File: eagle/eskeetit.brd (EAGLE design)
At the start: 47 x 28 mm, 46 parts, among them M1 WIRELESS-NRF24L01, U1 GY-521MPU6050, U2 TPS63000DRCR, Y1 20MHz

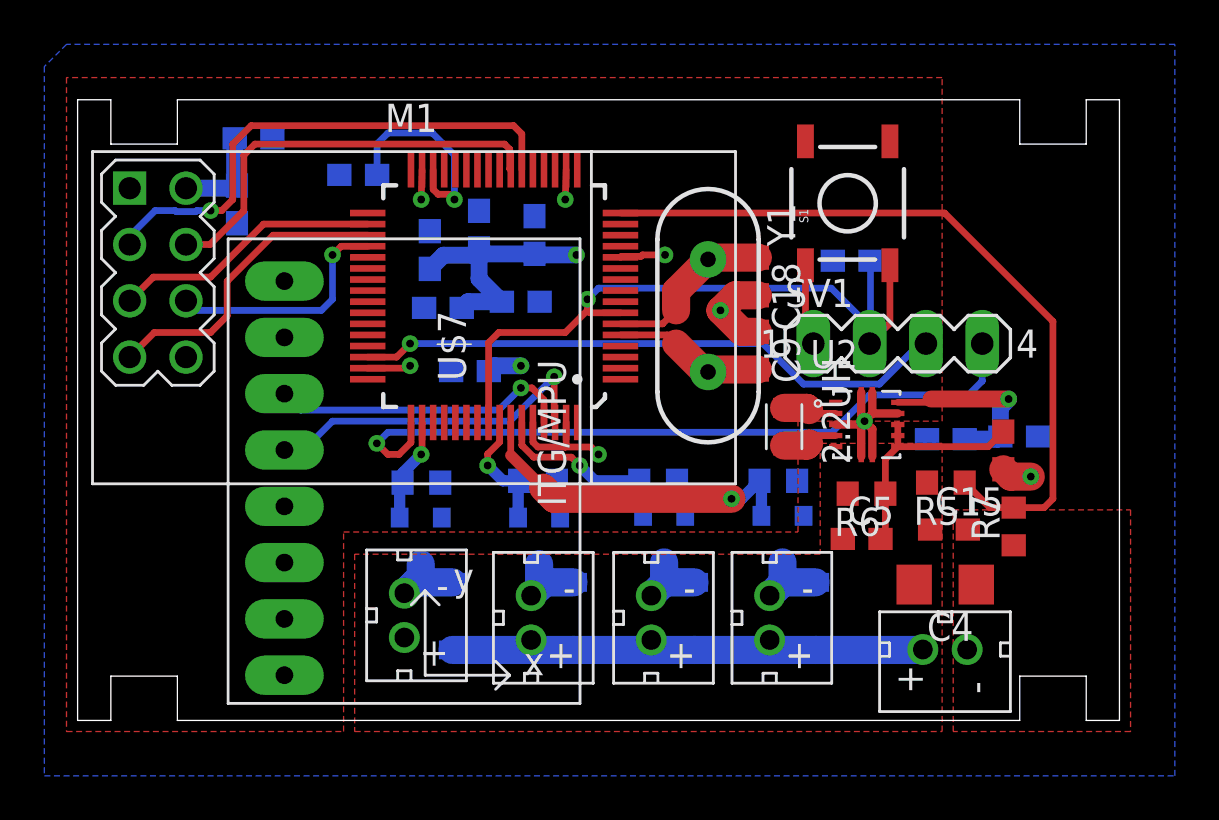
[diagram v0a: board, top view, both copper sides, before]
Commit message: changed PA5 to 20 mils, fixed some bottlenecks
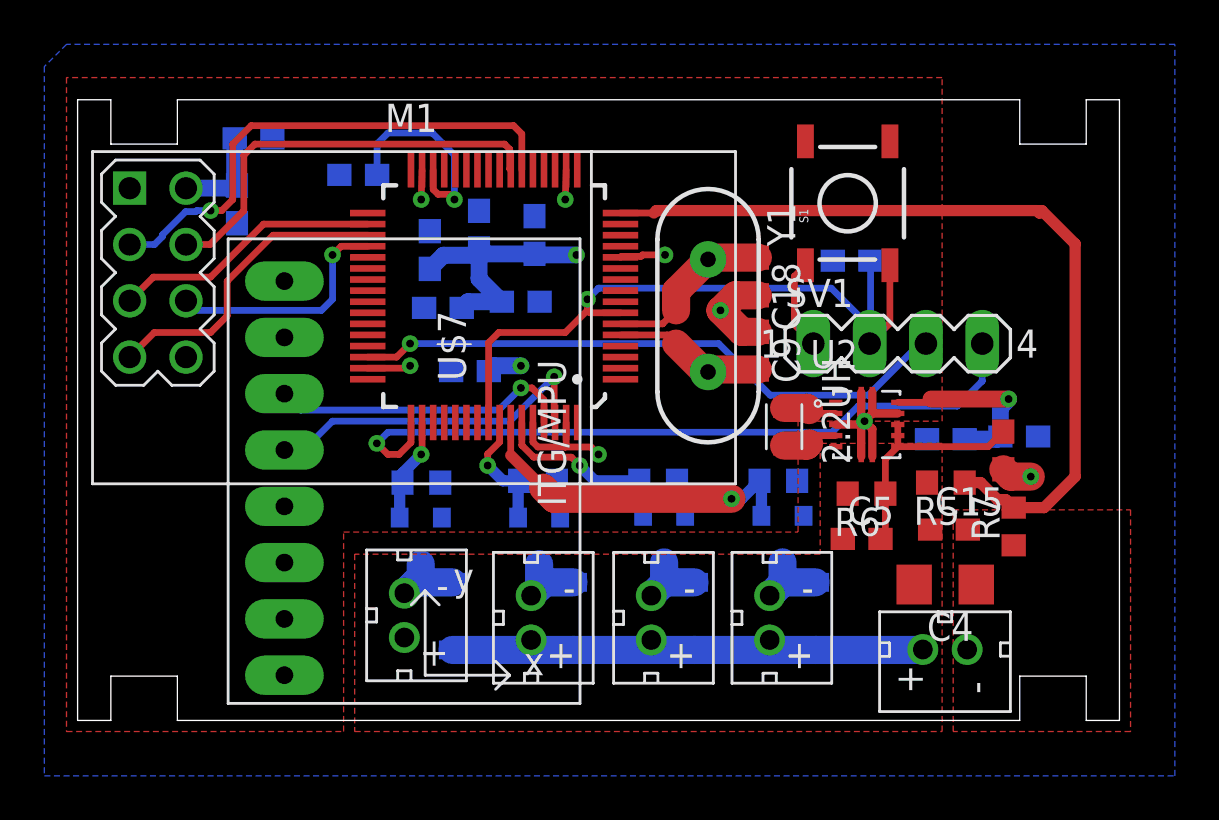
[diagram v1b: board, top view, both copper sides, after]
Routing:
- net PA5: track 34.1 -> 37.8 mm
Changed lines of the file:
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@@
 </polygon>
 <contactref element="SV1" pad="1"/>
-<wire x1="32.835" y1="20.536" x2="32.835" y2="17.355" width="0.3048" layer="1"/>
-<wire x1="32.835" y1="17.355" x2="33.19" y2="17" width="0.3048" layer="1"/>
+<wire x1="32.835" y1="20.536" x2="32.335" y2="20.036" width="0.3048" layer="1"/>
+<wire x1="32.335" y1="20.036" x2="32.335" y2="17.855" width="0.3048" layer="1"/>
+<wire x1="32.335" y1="17.855" x2="33.19" y2="17" width="0.3048" layer="1"/>
 <wire x1="13.09" y1="15.89" x2="14.89" y2="15.89" width="0.3048" layer="1"/>
 <wire x1="14.89" y1="15.89" x2="15" y2="16" width="0.3048" layer="1"/>
@@
 <contactref element="SV1" pad="3"/>
 <wire x1="38.27" y1="17" x2="38.0006875" y2="17" width="0.3048" layer="16"/>
-<wire x1="30.9193125" y1="17" x2="15" y2="17" width="0.3048" layer="16"/>
-<wire x1="38.0006875" y1="17" x2="36.1718875" y2="15.1712" width="0.3048" layer="16"/>
-<wire x1="32.7481125" y1="15.1712" x2="30.9193125" y2="17" width="0.3048" layer="16"/>
-<wire x1="36.1718875" y1="15.1712" x2="32.7481125" y2="15.1712" width="0.3048" layer="16"/>
+<wire x1="28.9193125" y1="17" x2="15" y2="17" width="0.3048" layer="16"/>
+<wire x1="38.0006875" y1="17" x2="35.6718875" y2="14.6712" width="0.3048" layer="16"/>
+<wire x1="31.2481125" y1="14.6712" x2="28.9193125" y2="17" width="0.3048" layer="16"/>
+<wire x1="35.6718875" y1="14.6712" x2="31.2481125" y2="14.6712" width="0.3048" layer="16"/>
 <via x="15" y="17" extent="1-16" drill="0.35"/>
 <wire x1="15" y1="17" x2="14.39" y2="16.39" width="0.3048" layer="1"/>
@@
 <contactref element="U$7" pad="49"/>
 <contactref element="SV1" pad="4"/>
-<wire x1="34.0340875" y1="13" x2="35.7170875" y2="14.683" width="0.3048" layer="16"/>
+<wire x1="34.0340875" y1="13" x2="35.2170875" y2="14.183" width="0.3048" layer="16"/>
 <wire x1="34.0340875" y1="13" x2="14" y2="13" width="0.3048" layer="16"/>
 <wire x1="14" y1="13" x2="13.5" y2="12.5" width="0.3048" layer="16"/>
@@
 <wire x1="15.04" y1="12.54" x2="15.04" y2="13.44" width="0.3048" layer="1"/>
 <wire x1="14.5" y1="12" x2="15.04" y2="12.54" width="0.3048" layer="1"/>
-<wire x1="35.7170875" y1="14.683" x2="40.183" y2="14.683" width="0.3048" layer="16"/>
+<wire x1="35.2170875" y1="14.183" x2="39.683" y2="14.183" width="0.3048" layer="16"/>
 <wire x1="40.81" y1="15.31" x2="40.81" y2="17" width="0.3048" layer="16"/>
-<wire x1="40.183" y1="14.683" x2="40.81" y2="15.31" width="0.3048" layer="16"/>
+<wire x1="39.683" y1="14.183" x2="40.81" y2="15.31" width="0.3048" layer="16"/>
 </signal>
 <signal name="SWDRST">
@@
 <wire x1="6.5" y1="23" x2="6" y2="23" width="0.3048" layer="1"/>
 <via x="6" y="23" extent="1-16" drill="0.35"/>
-<wire x1="6" y1="23" x2="5.377375" y2="23" width="0.3048" layer="16"/>
-<wire x1="5.377375" y1="23" x2="5.328575" y2="22.9512" width="0.3048" layer="16"/>
-<wire x1="5.328575" y1="22.9512" x2="4.451425" y2="22.9512" width="0.3048" layer="16"/>
-<wire x1="4.451425" y1="22.9512" x2="4.402625" y2="23" width="0.3048" layer="16"/>
-<wire x1="4.402625" y1="23" x2="3.5" y2="23" width="0.3048" layer="16"/>
-<wire x1="3.5" y1="23" x2="2.35" y2="21.85" width="0.3048" layer="16"/>
-<wire x1="2.35" y1="21.85" x2="2.35" y2="21.47" width="0.3048" layer="16"/>
+<wire x1="2.35" y1="21.47" x2="3.47" y2="21.47" width="0.3048" layer="16"/>
+<wire x1="3.47" y1="21.47" x2="3.8312" y2="21.8312" width="0.3048" layer="16"/>
+<wire x1="3.8312" y1="21.8312" x2="3.8312" y2="21.908575" width="0.3048" layer="16"/>
+<wire x1="3.8312" y1="21.908575" x2="4.873825" y2="22.9512" width="0.3048" layer="16"/>
+<wire x1="5.328575" y1="22.9512" x2="5.377375" y2="23" width="0.3048" layer="16"/>
+<wire x1="5.377375" y1="23" x2="6" y2="23" width="0.3048" layer="16"/>
+<wire x1="4.873825" y1="22.9512" x2="5.328575" y2="22.9512" width="0.3048" layer="16"/>
 </signal>
 <signal name="SPI2_CS">
@@
 <contactref element="R5" pad="1"/>
 <contactref element="R7" pad="2"/>
-<wire x1="40.02" y1="10.73" x2="41.15" y2="9.6" width="0.3048" layer="1"/>
-<wire x1="41.15" y1="9.6" x2="42.23" y2="9.6" width="0.3048" layer="1"/>
 <contactref element="U$7" pad="16"/>
-<wire x1="24.49" y1="22.89" x2="39.11" y2="22.89" width="0.3048" layer="1"/>
-<wire x1="39.11" y1="22.89" x2="44" y2="18" width="0.3048" layer="1"/>
-<wire x1="44" y1="18" x2="44" y2="10" width="0.3048" layer="1"/>
-<wire x1="43.6" y1="9.6" x2="42.23" y2="9.6" width="0.3048" layer="1"/>
-<wire x1="44" y1="10" x2="43.6" y2="9.6" width="0.3048" layer="1"/>
+<wire x1="42.23" y1="9.6" x2="41.8714" y2="9.9586" width="0.508" layer="1"/>
+<wire x1="40.7352625" y1="10.73" x2="40.02" y2="10.73" width="0.508" layer="1"/>
+<wire x1="41.8714" y1="9.9586" x2="41.5066625" y2="9.9586" width="0.508" layer="1"/>
+<wire x1="41.5066625" y1="9.9586" x2="40.7352625" y2="10.73" width="0.508" layer="1"/>
+<wire x1="42.23" y1="9.6" x2="43.6" y2="9.6" width="0.508" layer="1"/>
+<wire x1="45" y1="21.5" x2="43.5" y2="23" width="0.508" layer="1"/>
+<wire x1="43.6" y1="9.6" x2="45" y2="11" width="0.508" layer="1"/>
+<wire x1="45" y1="11" x2="45" y2="21.5" width="0.508" layer="1"/>
+<wire x1="43.39" y1="22.89" x2="43.5" y2="23" width="0.508" layer="1"/>
+<wire x1="26" y1="22.89" x2="24.49" y2="22.89" width="0.3048" layer="1"/>
+<wire x1="43.39" y1="22.89" x2="43.28" y2="23" width="0.508" layer="1"/>
+<wire x1="26.11" y1="23" x2="26" y2="22.89" width="0.508" layer="1"/>
+<wire x1="43.28" y1="23" x2="26.11" y2="23" width="0.508" layer="1"/>
+<wire x1="26" y1="22.89" x2="26" y2="22.89" width="0.3048" layer="1"/>
 </signal>
 </signals>

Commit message: PCB Notes, first remote revisions (Vaibhav)
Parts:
- moved C1 2.56 mm to (9.74, 24.4), turned to 90 degrees
- moved 2.2UH 1.50 mm to (31.9, 11.8)
- moved SV1 1.41 mm to (38.0, 18.0)
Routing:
- net 3.3V: track 26.5 -> 56.0 mm, vias 3 -> 8
- net PWR: track 21.2 -> 8.89 mm
- net PA5: track 37.8 -> 34.4 mm
- net GND: track 29.9 -> 32.8 mm, vias 8 -> 10
- net SPI2_CE: track 23.2 -> 21.7 mm
- net SPI2_CS: track 19.0 -> 17.5 mm
- net SWDCLK: track 33.0 -> 34.4 mm
- net SWDIO: track 27.4 -> 28.4 mm
- net N$1: track 2.52 -> 3.41 mm
